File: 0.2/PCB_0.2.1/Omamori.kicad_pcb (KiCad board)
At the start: 2 copper layers, 25 x 35 mm, 29 parts, among them J1 Conn_01x04_Female, U1 BQ25504, U2 TPS61222DCK, U3 ATtiny85, U4 TS-1233

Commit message: Updated 0.2.1 PCB design.
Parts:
- removed D2: DIODE, Diode_SMD:D_SOD-323_HandSoldering
- added Q1: IRLML0030, Package_TO_SOT_SMD:SOT-23, B.Cu at (34.5, 40.9)
- added R_oc3: 1.8M, Resistor_SMD:R_0603_1608Metric_Pad0.98x0.95mm_HandSolder, B.Cu at (34.3, 44.5)
- added R_oc4: 8.2M, Resistor_SMD:R_0603_1608Metric_Pad0.98x0.95mm_HandSolder, B.Cu at (32.8, 44.5)
- added R_oc5: 10M, Resistor_SMD:R_0603_1608Metric_Pad0.98x0.95mm_HandSolder, B.Cu at (31.2, 44.5)
- moved C_pre_boost1 0.20 mm to (21.3, 22.6)
- moved C_filter1 0.14 mm to (22.9, 22.5)
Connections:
- C_filter1 pad 1: /Vstor -> Net-(C_filter1-Pad1)
- C_pre_boost1 pad 1: /Vstor -> Net-(C_filter1-Pad1)
- L_boost1 pad 1: /Vstor -> Net-(C_filter1-Pad1)
- U1 pad 15: /Vstor -> (no net)
- U2 pad 1: /Vstor -> Net-(C_filter1-Pad1)
- U2 pad 6: /Vbat_ok -> Net-(C_filter1-Pad1)
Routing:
- net Net-(C_filter1-Pad1): track 0.00 -> 42.2 mm, vias 0 -> 2
- net /Vmeasure: track 2.30 -> 27.4 mm
- net /Vstor: track 21.1 -> 0.00 mm
- net GND: track 132.7 -> 146.5 mm
- net /Vr_div: track 8.90 -> 16.1 mm
- net Net-(C_super1-Pad1): track 34.1 -> 39.8 mm
- net Net-(Sol_1-Pad2): track 35.6 -> 38.9 mm
- net /Din_LED: track 2.01 -> 4.82 mm, vias 1 -> 2
- net Net-(R_oc4-Pad1): track 0.00 -> 1.52 mm
- net /Vbat_ok: track 16.7 -> 17.9 mm
- net /Vcc_ATTiny: track 39.2 -> 39.9 mm

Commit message: Updated pcb design and gerber files.
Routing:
- net Net-(C_super1-Pad1): track 39.8 -> 21.3 mm, vias 2 -> 0
- net GND: track 146.5 -> 152.8 mm, vias 4 -> 5
- net /Vmeasure: track 27.4 -> 29.8 mm

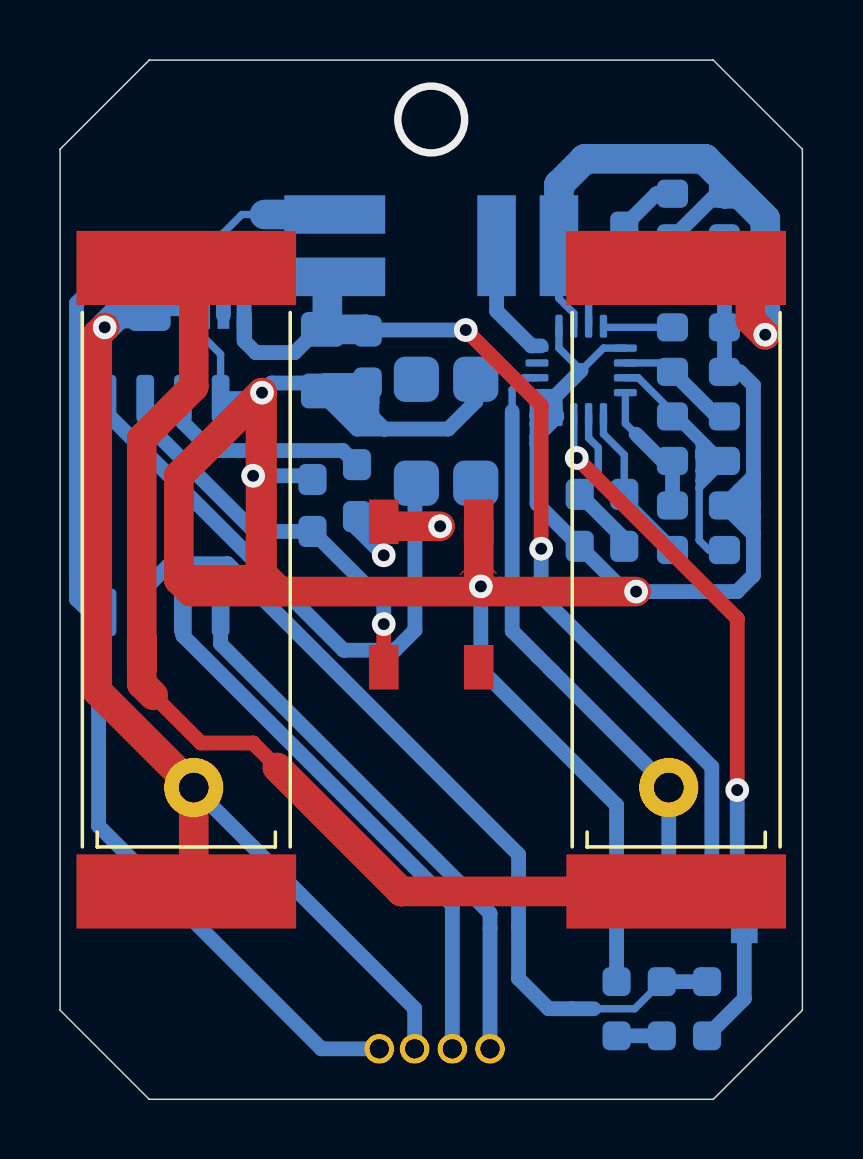
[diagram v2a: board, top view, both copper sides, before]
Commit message: Layout and Design redesign.
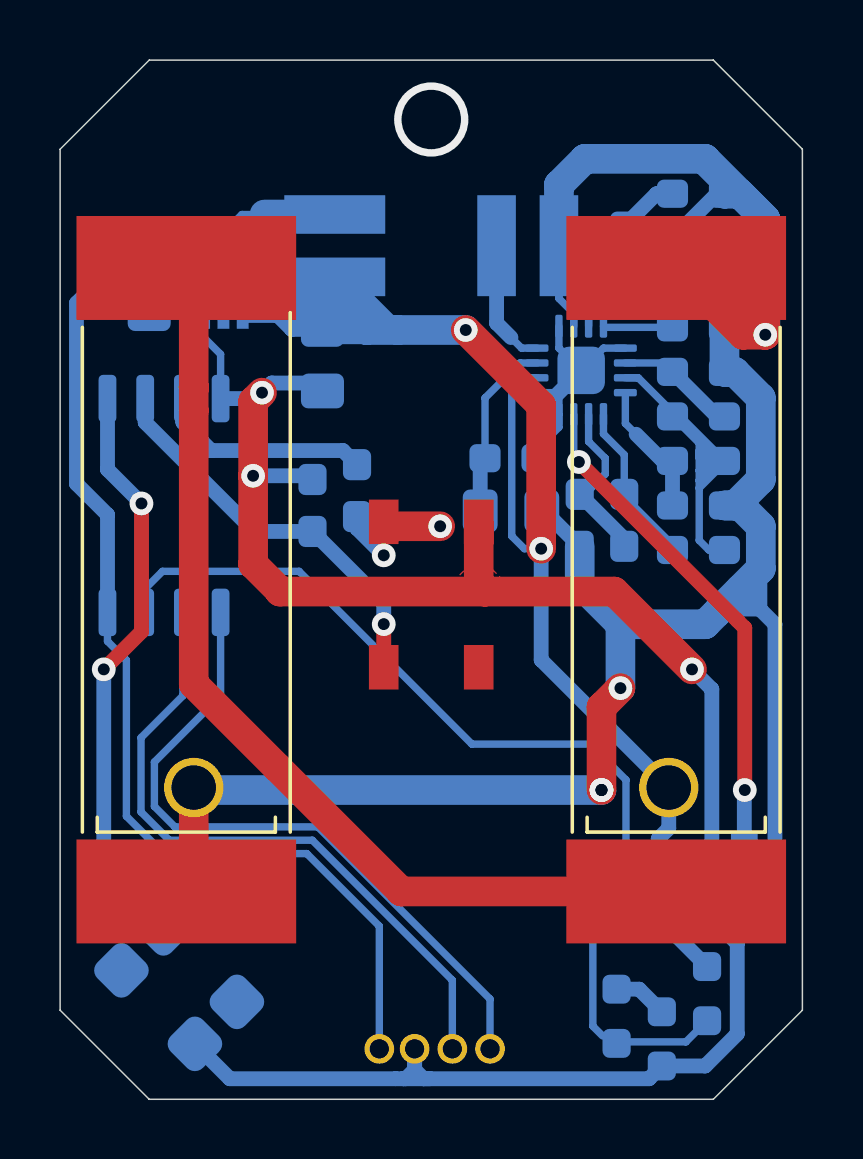
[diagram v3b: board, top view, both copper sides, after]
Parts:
- added C_Stor1: 10uF, Capacitor_SMD:C_0805_2012Metric_Pad1.18x1.45mm_HandSolder, B.Cu at (27.7, 27.7)
- moved U4 20.7 mm to (16.5, 43.7), turned to 135 degrees
- moved C_filter1 5.91 mm to (27.7, 25.9), turned to 0 degrees
- moved R_oc5 1.83 mm to (32.8, 45.5), turned to 90 degrees
- moved R_oc4 1.55 mm to (31.2, 44.7), turned to 270 degrees
- moved Q1 1.02 mm to (34.5, 39.9)
- moved R_oc3 0.51 mm to (34.3, 43.9), turned to 270 degrees
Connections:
- C_filter1 pad 1: Net-(C_filter1-Pad1) -> Net-(C_Stor1-Pad1)
- C_led1 pad 2: GND -> /FAKE_GND
- C_post_boost1 pad 2: GND -> /FAKE_GND
- C_pre_boost1 pad 1: Net-(C_filter1-Pad1) -> Net-(C_pre_boost1-Pad1)
- C_pre_boost1 pad 2: GND -> /FAKE_GND
- C_super1 pad 1: Net-(C_super1-Pad1) -> Net-(C_pre_boost1-Pad1)
- D1 pad 1: GND -> /FAKE_GND
- J1 pad 4: GND -> /FAKE_GND
- L_boost1 pad 1: Net-(C_filter1-Pad1) -> Net-(C_pre_boost1-Pad1)
- Q1 pad 2: Net-(C_filter1-Pad1) -> GND
- Q1 pad 3: Net-(C_super1-Pad1) -> /FAKE_GND
- R_oc3 pad 1: Net-(C_filter1-Pad1) -> Net-(C_pre_boost1-Pad1)
- R_oc5 pad 1: GND -> /FAKE_GND
- U1 pad 14: Net-(C_super1-Pad1) -> Net-(C_pre_boost1-Pad1)
- U1 pad 15: (no net) -> Net-(C_Stor1-Pad1)
- U2 pad 1: Net-(C_filter1-Pad1) -> Net-(C_pre_boost1-Pad1)
- U2 pad 3: GND -> /FAKE_GND
- U2 pad 6: Net-(C_filter1-Pad1) -> Net-(C_pre_boost1-Pad1)
- U3 pad 4: GND -> /FAKE_GND
- U4 pad 3: GND -> /FAKE_GND
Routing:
- net GND: track 152.8 -> 77.3 mm, vias 5 -> 3
- net /FAKE_GND: track 0.00 -> 74.2 mm, vias 0 -> 3
- net Net-(C_pre_boost1-Pad1): track 0.00 -> 60.0 mm, vias 0 -> 2
- net Net-(C_filter1-Pad1): track 42.2 -> 0.00 mm, vias 2 -> 0
- net Net-(C_super1-Pad1): track 21.3 -> 0.00 mm
- net /Vsolar: track 28.0 -> 34.4 mm
- net Net-(C_Stor1-Pad1): track 0.00 -> 6.11 mm
- net Net-(Sol_1-Pad2): track 38.9 -> 33.2 mm
- net /Tx: track 18.5 -> 23.1 mm
- net /Rx: track 18.5 -> 22.5 mm
- net /Vmeasure: track 29.8 -> 33.2 mm
- net /Vbat_ok: track 17.9 -> 16.6 mm
- net /Reset: track 20.0 -> 20.2 mm, vias 0 -> 2
- added copper zone on F.Cu, net /FAKE_GND
- removed copper zone on F.Cu, net GND

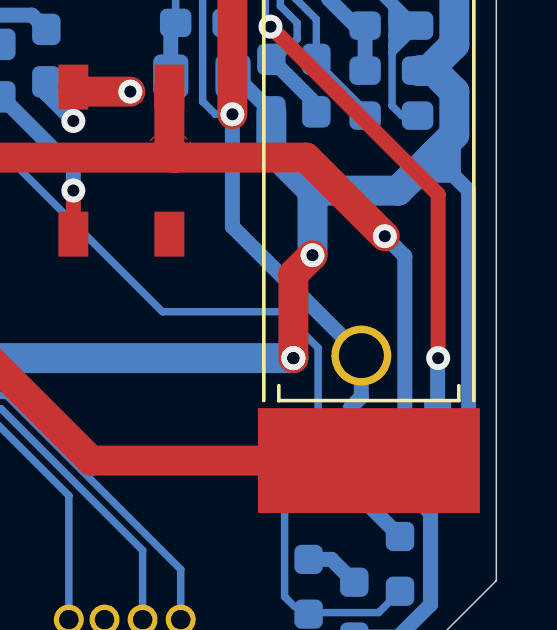
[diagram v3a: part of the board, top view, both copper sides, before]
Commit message: Added pull down resistor.
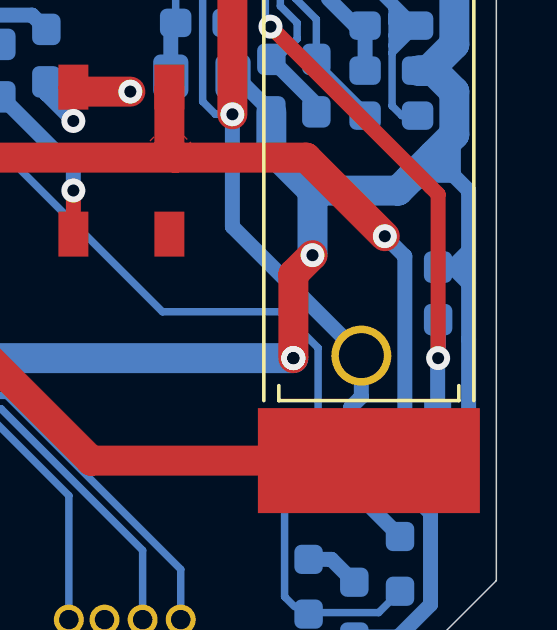
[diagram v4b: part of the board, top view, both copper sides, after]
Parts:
- added R_pulldown1: 10M, Resistor_SMD:R_0603_1608Metric_Pad1.05x0.95mm_HandSolder, B.Cu at (35.6, 34.9)
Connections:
- D1 pad 4: (no net) -> Net-(D1-Pad4)
- U4 pad 1: (no net) -> Net-(U4-Pad1)
- U4 pad 4: (no net) -> Net-(U4-Pad4)
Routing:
- net GND: track 77.3 -> 79.3 mm
- net /Vbat_ok: track 16.6 -> 17.9 mm
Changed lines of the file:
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@@
-(kicad_pcb (version 20171130) (host pcbnew "(5.1.9)-1")
+(kicad_pcb (version 20171130) (host pcbnew 5.1.5+dfsg1-2build2)
   (general
     (thickness 1.6)
     (drawings 10)
-    (tracks 364)
+    (tracks 369)
     (zones 0)
-    (modules 33)
-    (nets 27)
+    (modules 34)
+    (nets 30)
   )
   (page A4)
@@
   )
   (setup
-    (last_trace_width 0.25)
+    (last_trace_width 0.5)
     (user_trace_width 0.5)
     (user_trace_width 1)
@@
   (net 25 "Net-(C_pre_boost1-Pad1)")
   (net 26 /FAKE_GND)
+  (net 27 "Net-(D1-Pad4)")
+  (net 28 "Net-(U4-Pad1)")
+  (net 29 "Net-(U4-Pad4)")
   (net_class Default "This is the default net class."
     (clearance 0.2)
@@
     (add_net "Net-(C_pre_boost1-Pad1)")
     (add_net "Net-(C_ref1-Pad1)")
+    (add_net "Net-(D1-Pad4)")
     (add_net "Net-(L_boost1-Pad2)")
     (add_net "Net-(L_bst1-Pad2)")
@@
     (add_net "Net-(R_uv1-Pad1)")
     (add_net "Net-(Sol_1-Pad2)")
+    (add_net "Net-(U4-Pad1)")
+    (add_net "Net-(U4-Pad4)")
+  )
+  (module Resistor_SMD:R_0603_1608Metric_Pad1.05x0.95mm_HandSolder (layer B.Cu)
+    (at 35.56 34.925 270)
+    (descr "Resistor SMD 0603 (1608 Metric), square (rectangular) end terminal, IPC_7351 nominal with elongated pad for handsoldering. (Body size source: http://www.tortai-tech.com/upload/download/2011102023233369053.pdf), generated with kicad-footprint-generator")
+    (tags "resistor handsolder")
+    (attr smd)
+    (fp_text reference R_pulldown1 (at 0 1.43 270) (layer B.SilkS) hide
+      (effects (font (size 1 1) (thickness 0.15)) (justify mirror))
+    )
+    (fp_text value 10M (at 0 -1.43 270) (layer B.Fab) hide
+      (effects (font (size 1 1) (thickness 0.15)) (justify mirror))
+    )
+    (fp_text user %R (at 0 0 270) (layer B.Fab) hide
+      (effects (font (size 0.4 0.4) (thickness 0.06)) (justify mirror))
+    )
+    (fp_line (start 1.65 -0.73) (end -1.65 -0.73) (layer B.CrtYd) (width 0.05))
+    (fp_line (start 1.65 0.73) (end 1.65 -0.73) (layer B.CrtYd) (width 0.05))
+    (fp_line (start -1.65 0.73) (end 1.65 0.73) (layer B.CrtYd) (width 0.05))
+    (fp_line (start -1.65 -0.73) (end -1.65 0.73) (layer B.CrtYd) (width 0.05))
+    (fp_line (start -0.171267 -0.51) (end 0.171267 -0.51) (layer B.SilkS) (width 0.12))
+    (fp_line (start -0.171267 0.51) (end 0.171267 0.51) (layer B.SilkS) (width 0.12))
+    (fp_line (start 0.8 -0.4) (end -0.8 -0.4) (layer B.Fab) (width 0.1))
+    (fp_line (start 0.8 0.4) (end 0.8 -0.4) (layer B.Fab) (width 0.1))
+    (fp_line (start -0.8 0.4) (end 0.8 0.4) (layer B.Fab) (width 0.1))
+    (fp_line (start -0.8 -0.4) (end -0.8 0.4) (layer B.Fab) (width 0.1))
+    (pad 2 smd roundrect (at 0.875 0 270) (size 1.05 0.95) (layers B.Cu B.Paste B.Mask) (roundrect_rratio 0.25)
+      (net 11 /Vbat_ok))
+    (pad 1 smd roundrect (at -0.875 0 270) (size 1.05 0.95) (layers B.Cu B.Paste B.Mask) (roundrect_rratio 0.25)
+      (net 1 GND))
+    (model ${KISYS3DMOD}/Resistor_SMD.3dshapes/R_0603_1608Metric.wrl
+      (at (xyz 0 0 0))
+      (scale (xyz 1 1 1))
+      (rotate (xyz 0 0 0))
+    )
   )
   (module Resistor_SMD:R_0603_1608Metric_Pad0.98x0.95mm_HandSolder (layer B.Cu)
@@
     (pad 3 smd roundrect (at -1.75 -1 135) (size 1.524 1.524) (layers B.Cu B.Paste B.Mask) (roundrect_rratio 0.25)
       (net 26 /FAKE_GND))
-    (pad 1 smd roundrect (at -1.75 1 135) (size 1.524 1.524) (layers B.Cu B.Paste B.Mask) (roundrect_rratio 0.25))
+    (pad 1 smd roundrect (at -1.75 1 135) (size 1.524 1.524) (layers B.Cu B.Paste B.Mask) (roundrect_rratio 0.25)
+      (net 28 "Net-(U4-Pad1)"))
     (pad 2 smd roundrect (at 1.75 1 135) (size 1.524 1.524) (layers B.Cu B.Paste B.Mask) (roundrect_rratio 0.25)
       (net 17 /Reset))
-    (pad 4 smd roundrect (at 1.75 -1 135) (size 1.524 1.524) (layers B.Cu B.Paste B.Mask) (roundrect_rratio 0.25))
+    (pad 4 smd roundrect (at 1.75 -1 135) (size 1.524 1.524) (layers B.Cu B.Paste B.Mask) (roundrect_rratio 0.25)
+      (net 29 "Net-(U4-Pad4)"))
   )
   (module Inductor_SMD:L_Wuerth_MAPI-3015 (layer B.Cu)
@@
     (pad 2 smd rect (at 2.45 -1.6 90) (size 1.5 1) (layers F.Cu F.Paste F.Mask)
       (net 13 /Din_LED))
-    (pad 4 smd rect (at -2.45 1.6 90) (size 1.5 1) (layers F.Cu F.Paste F.Mask))
+    (pad 4 smd rect (at -2.45 1.6 90) (size 1.5 1) (layers F.Cu F.Paste F.Mask)
+      (net 27 "Net-(D1-Pad4)"))
     (pad 3 smd rect (at -2.45 -1.6 90) (size 1.5 1) (layers F.Cu F.Paste F.Mask)
       (net 12 /Vcc_LED))
@@
   (segment (start 36.10001 29.62583) (end 35.40292 30.32292) (width 1) (layer B.Cu) (net 1))
   (segment (start 36.576 39.796) (end 35.544 40.828) (width 0.5) (layer B.Cu) (net 1))
-  (segment (start 36.576 31.496) (end 36.576 39.796) (width 0.5) (layer B.Cu) (net 1))
   (segment (start 28.5625 24.51249) (end 28.5625 23.85) (width 0.5) (layer B.Cu) (net 1))
   (segment (start 28.5625 24.4375) (end 29 24) (width 0.5) (layer B.Cu) (net 1))
@@
   (segment (start 34.64092 31.08492) (end 34.225839 31.500001) (width 1) (layer B.Cu) (net 1))
   (segment (start 35.40292 30.32292) (end 34.64092 31.08492) (width 1) (layer B.Cu) (net 1))
+  (segment (start 36.035 34.05) (end 36.576 34.591) (width 0.5) (layer B.Cu) (net 1))
+  (segment (start 36.576 36.449) (end 36.576 39.796) (width 0.5) (layer B.Cu) (net 1))
+  (segment (start 36.576 31.496) (end 36.576 36.449) (width 0.5) (layer B.Cu) (net 1))
+  (segment (start 36.035 34.05) (end 36.576 33.509) (width 0.5) (layer B.Cu) (net 1))
+  (segment (start 35.56 34.05) (end 36.035 34.05) (width 0.5) (layer B.Cu) (net 1))
   (segment (start 30.8375 21.5) (end 30.8 21.4625) (width 0.25) (layer B.Cu) (net 2))
   (segment (start 33.125 21.5) (end 30.8375 21.5) (width 0.25) (layer B.Cu) (net 2))
@@
   (segment (start 29.8 25.863) (end 29.972 26.035) (width 0.25) (layer B.Cu) (net 11))
   (segment (start 29.8 24.4375) (end 29.8 25.863) (width 0.25) (layer B.Cu) (net 11))
+  (segment (start 35.56 37.084) (end 35.56 35.8) (width 0.5) (layer B.Cu) (net 11))
   (segment (start 23.35 33) (end 23.4 32.95) (width 0.25) (layer F.Cu) (net 12))
   (segment (start 23.4 32.95) (end 23.2 32.95) (width 0.25) (layer F.Cu) (net 12))
@@
   (segment (start 32.004 43.7915) (end 32.766 44.5535) (width 0.5) (layer B.Cu) (net 23))
   (segment (start 31.242 43.7915) (end 32.004 43.7915) (width 0.5) (layer B.Cu) (net 23))
+  (segment (start 26.6485 26.0705) (end 26.811 25.908) (width 0.5) (layer B.Cu) (net 24))
+  (segment (start 26.6485 27.686) (end 26.6485 26.0705) (width 0.5) (layer B.Cu) (net 24))
+  (segment (start 26.811 23.879568) (end 26.811 25.908) (width 0.25) (layer B.Cu) (net 24))
+  (segment (start 27.990568 22.7) (end 26.811 23.879568) (width 0.25) (layer B.Cu) (net 24))
+  (segment (start 28.5625 22.7) (end 27.990568 22.7) (width 0.25) (layer B.Cu) (net 24))
   (segment (start 18.65 21.1) (end 18.65 20.975) (width 0.25) (layer B.Cu) (net 25))
   (segment (start 18.725001 18.824999) (end 18.65 18.9) (width 0.25) (layer B.Cu) (net 25))
@@
   (segment (start 28.702 24.13) (end 26.162 21.59) (width 1) (layer F.Cu) (net 25))
   (segment (start 28.702 28.956) (end 28.702 24.13) (width 1) (layer F.Cu) (net 25))
-  (segment (start 26.6485 26.0705) (end 26.811 25.908) (width 0.5) (layer B.Cu) (net 24))
-  (segment (start 26.6485 27.686) (end 26.6485 26.0705) (width 0.5) (layer B.Cu) (net 24))
-  (segment (start 26.811 23.879568) (end 26.811 25.908) (width 0.25) (layer B.Cu) (net 24))
-  (segment (start 27.990568 22.7) (end 26.811 23.879568) (width 0.25) (layer B.Cu) (net 24))
-  (segment (start 28.5625 22.7) (end 27.990568 22.7) (width 0.25) (layer B.Cu) (net 24))
   (segment (start 33.125 36.875) (end 33 37) (width 0.25) (layer B.Cu) (net 25))
   (segment (start 33.29 37.29) (end 33 37) (width 0.5) (layer B.Cu) (net 25))

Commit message: Minor Layout update.
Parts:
- R_oc1: value 6.2M -> 5.6M
- R_oc2: value 3.9M -> 4.3M
- moved C_Stor1 4.45 mm to (25.0, 24.1), turned to 270 degrees
- moved C_filter1 2.22 mm to (26.8, 23.9), turned to 270 degrees
- moved R_oc5 0.76 mm to (32.8, 44.7)
- moved R_oc3 0.13 mm to (34.3, 43.8)
- moved C_pre_boost1 0.13 mm to (21.3, 22.7)
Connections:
- net /FAKE_GND renamed /Drain
- net Net-(C_pre_boost1-Pad1) renamed /Vbat
- D1 pad 4: Net-(D1-Pad4) -> (no net)
- U4 pad 1: Net-(U4-Pad1) -> (no net)
- U4 pad 4: Net-(U4-Pad4) -> (no net)
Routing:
- net GND: track 79.3 -> 173.6 mm, vias 3 -> 4
- net /Vbat: track 60.0 -> 86.7 mm
- net Net-(L_boost1-Pad2): track 4.59 -> 25.4 mm
- net /Drain: track 74.2 -> 81.6 mm
- net /Tx: track 23.1 -> 18.5 mm
- net /Rx: track 22.5 -> 18.5 mm
- net /Vmeasure: track 33.2 -> 30.3 mm
- net Net-(Sol_1-Pad2): track 33.2 -> 30.7 mm
- net Net-(C_Stor1-Pad1): track 6.11 -> 3.71 mm
- net /Vcc_ATTiny: track 39.6 -> 37.2 mm
- net /Din_LED: track 4.82 -> 3.17 mm, vias 2 -> 1
- removed copper zone on F.Cu, net /Drain
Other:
- rule via_min_size: 0.4 -> 0.2

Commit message: Final Version of v0.2 22.12.2021.
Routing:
- net Net-(L_bst1-Pad2): track 4.32 -> 16.6 mm
- net /Vsolar: track 34.4 -> 40.9 mm

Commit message: Added Interactive BOM. Updated Gerber Files.
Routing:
- net /Vbat: track 86.7 -> 84.7 mm
